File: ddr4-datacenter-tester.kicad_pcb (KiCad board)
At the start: 10 copper layers, 152.9 x 90 mm, 304 parts, among them IC1 TPS54561, IC3 TPD8S009DSMR, J1 0878311420, J10 61300311121, J3 DC_SOCKET, J4 WE_629105150521, J6 685119134923, J7 1140084168, J8 61300311121, Q2 BSS138APW, Q3 BSS138APW, Q4 BSS138APW, Q5 BSS138APW, Q6 BSS138APW, Q7 BSS138APW, Q8 BSS138APW, U10 LM3881MME_NOPB, U11 S27KL0641DABHI023, U12 TPS62823DLCT, U14 2199155-1, U15 XC7K160T-FFG676, U3 S25FL128SAGNFI000, U4 TPS65296, U5 TPS62823DLCT, U6 KSZ9031RNXCA, U7 FT4232HQ, U8 SRST, U9 TPS62823DLCT, Y1 ABM8G-25.000MHZ-18-D2Y-T, Y2 ABM8G-12.000MHZ-18-D2Y-T

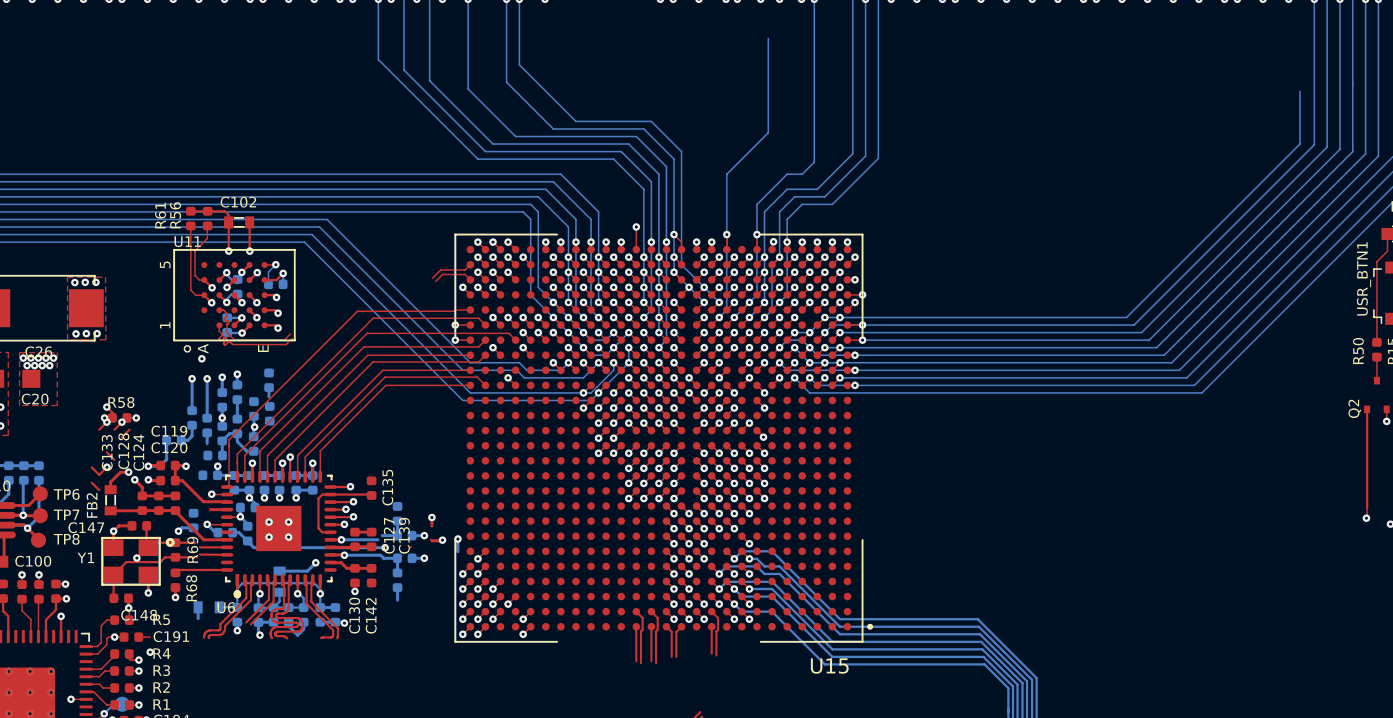
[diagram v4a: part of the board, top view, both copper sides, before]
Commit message: Add hyper ram routing
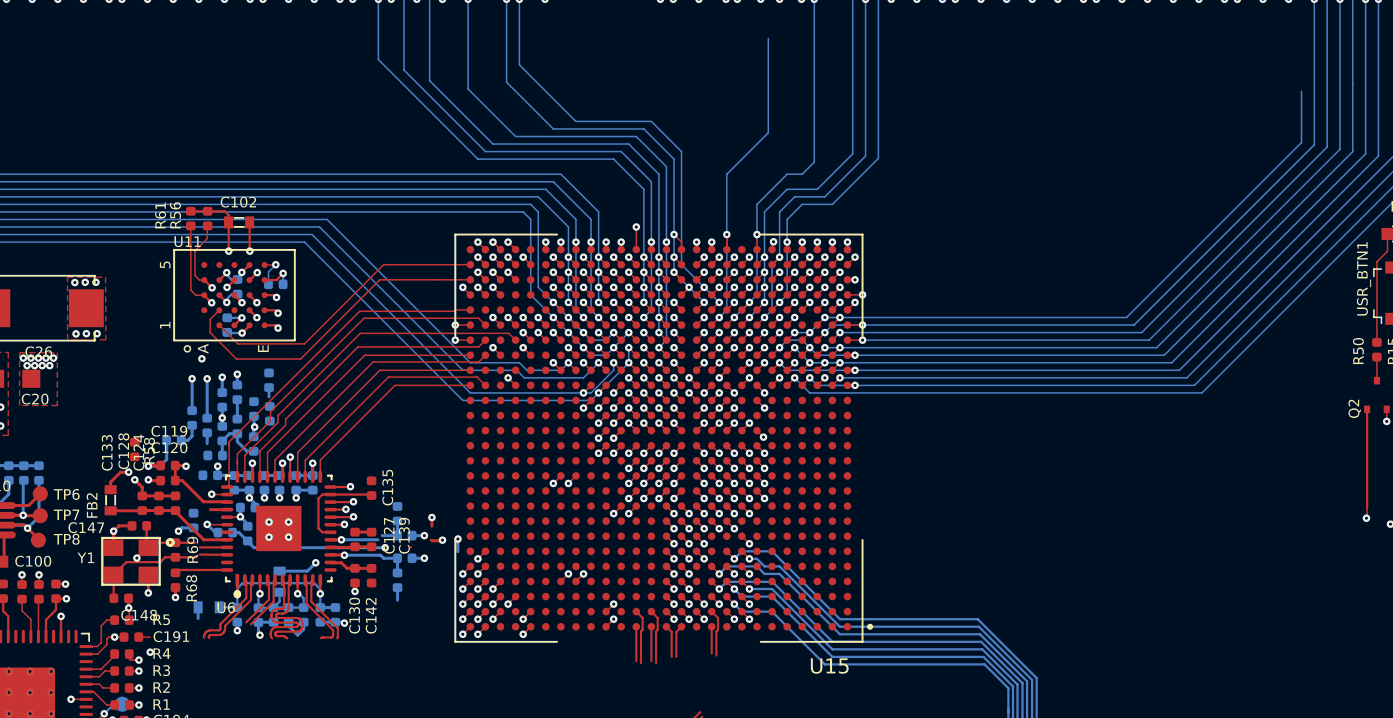
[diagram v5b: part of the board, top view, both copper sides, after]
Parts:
- moved R58 2.32 mm to (148.9, 90.8), turned to 90 degrees
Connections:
- U15 pad AC8: Net-(U15-PadAC8) -> DQS17_T
- U15 pad AD8: Net-(U15-PadAD8) -> DQS17_C
- U15 pad B18: 3V3_SYS -> VDDQ
- U15 pad E19: 3V3_SYS -> VDDQ
- U15 pad F16: 3V3_SYS -> VDDQ
- U15 pad H20: 3V3_SYS -> VDDQ
- U15 pad J17: 3V3_SYS -> VDDQ
- U15 pad K24: 3V3_SYS -> VDDQ
- U15 pad M18: 3V3_SYS -> VDDQ
- U15 pad N25: 3V3_SYS -> VDDQ
- U15 pad P22: 3V3_SYS -> VDDQ
- U15 pad R19: 3V3_SYS -> VDDQ
- U15 pad T16: 3V3_SYS -> VDDQ
- U15 pad T26: 3V3_SYS -> VDDQ
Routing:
- net HR_CKP: track 9.49 -> 21.9 mm
- net HR_RST: track 19.6 -> 30.5 mm
- net HR_CKN: track 9.89 -> 19.3 mm
- net HR_RW: track 13.3 -> 22.7 mm
- net HR_DQ4: track 12.1 -> 21.4 mm
- net HR_CS: track 18.2 -> 26.9 mm
- net HR_DQ2: track 12.2 -> 20.9 mm
- net HR_DQ3: track 13.7 -> 22.4 mm
- net HR_DQ0: track 11.5 -> 19.8 mm
- net HR_DQ5: track 8.81 -> 16.4 mm, vias 3 -> 2
- net HR_DQ7: track 10.8 -> 17.8 mm
- net Net-(U15-PadAD4): track 20.3 -> 25.2 mm
- net HR_DQ6: track 12.2 -> 16.5 mm
- net Net-(U15-PadAE11): track 15.5 -> 11.7 mm
- net HR_DQ1: track 15.5 -> 18.3 mm
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
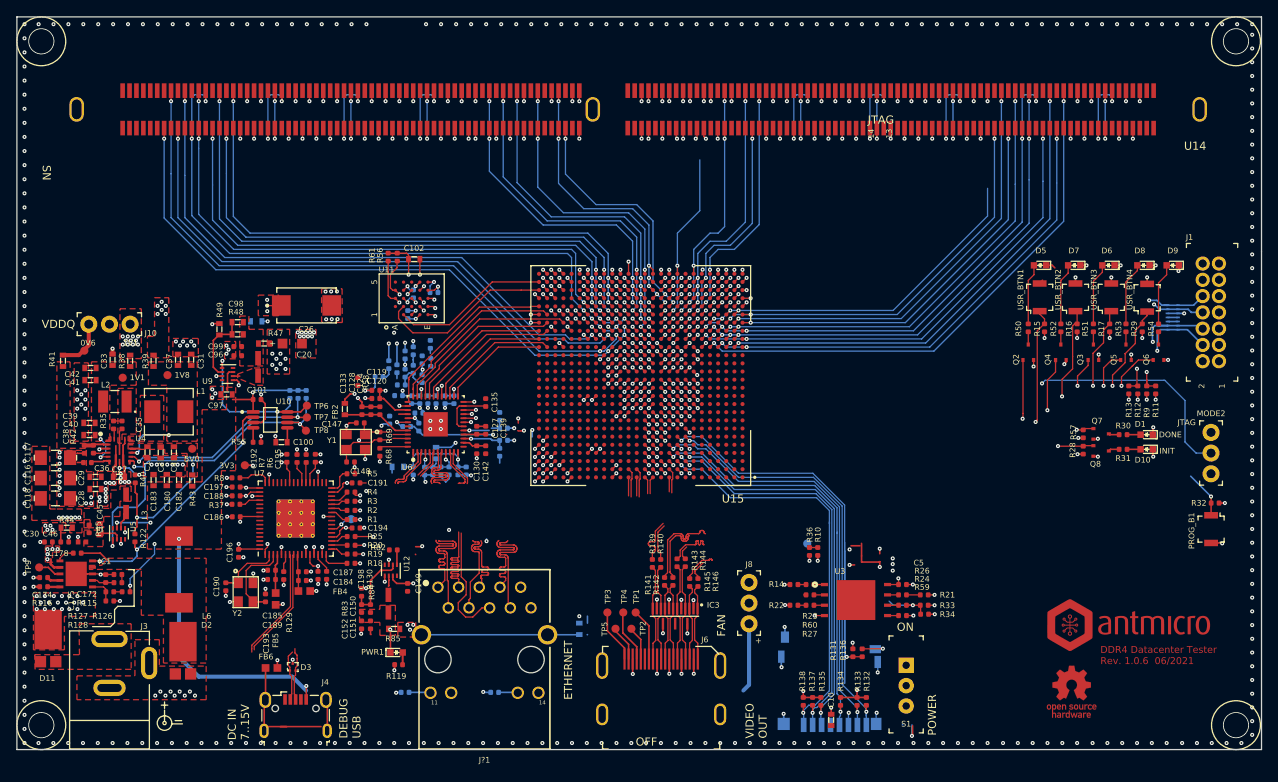
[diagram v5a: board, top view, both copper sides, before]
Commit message: Add DQS[9:17] redundant connection
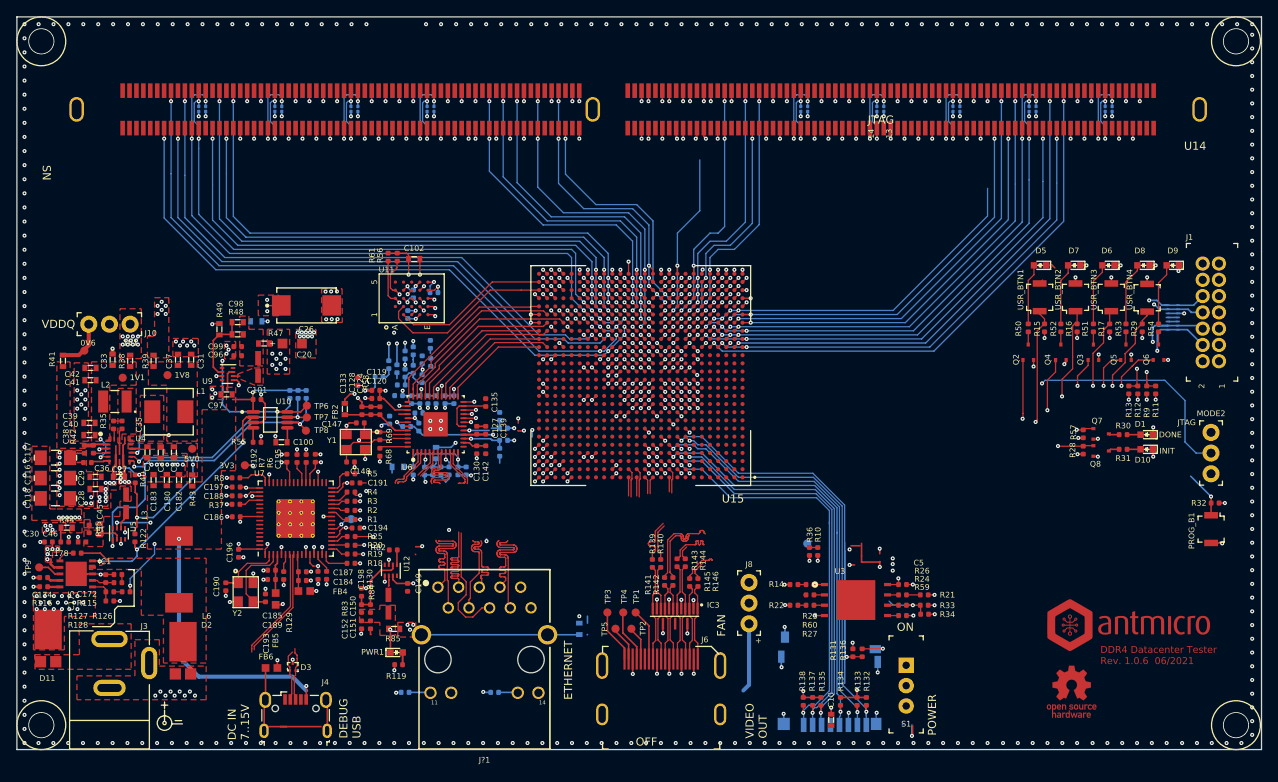
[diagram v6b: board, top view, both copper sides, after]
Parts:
- added R117: R_0R_0201, ddr4-datacenter-tester-footprints:0201-res, B.Cu at (130.2, 57.3)
- added R118: R_0R_0201, ddr4-datacenter-tester-footprints:0201-res, B.Cu at (129.3, 57.3)
- added R120: R_0R_0201, ddr4-datacenter-tester-footprints:0201-res, B.Cu at (148.9, 57.3)
- added R121: R_0R_0201, ddr4-datacenter-tester-footprints:0201-res, B.Cu at (148.0, 57.3)
- added R123: R_0R_0201, ddr4-datacenter-tester-footprints:0201-res, B.Cu at (158.2, 57.3)
- added R124: R_0R_0201, ddr4-datacenter-tester-footprints:0201-res, B.Cu at (157.4, 57.3)
- added R125: R_0R_0201, ddr4-datacenter-tester-footprints:0201-res, B.Cu at (139.5, 57.3)
- added R147: R_0R_0201, ddr4-datacenter-tester-footprints:0201-res, B.Cu at (138.7, 57.3)
- added R148: R_0R_0201, ddr4-datacenter-tester-footprints:0201-res, B.Cu at (241.5, 57.3)
- added R149: R_0R_0201, ddr4-datacenter-tester-footprints:0201-res, B.Cu at (240.7, 57.3)
- added R150: R_0R_0201, ddr4-datacenter-tester-footprints:0201-res, B.Cu at (213.5, 57.3)
- added R151: R_0R_0201, ddr4-datacenter-tester-footprints:0201-res, B.Cu at (212.6, 57.3)
- added R152: R_0R_0201, ddr4-datacenter-tester-footprints:0201-res, B.Cu at (232.2, 57.3)
- added R153: R_0R_0201, ddr4-datacenter-tester-footprints:0201-res, B.Cu at (231.3, 57.3)
- added R154: R_0R_0201, ddr4-datacenter-tester-footprints:0201-res, B.Cu at (222.8, 57.3)
- added R155: R_0R_0201, ddr4-datacenter-tester-footprints:0201-res, B.Cu at (222.0, 57.3)
- added R156: R_0R_0201, ddr4-datacenter-tester-footprints:0201-res, B.Cu at (204.1, 57.3)
- added R157: R_0R_0201, ddr4-datacenter-tester-footprints:0201-res, B.Cu at (203.3, 57.3)
- R100, R101, R102, R103, R104, R105, R106, R107, R108, R109, R110, R111, R112, R113, R114, R97, R98, R99: footprint antmicro-footprints:0201-res -> ddr4-datacenter-tester-footprints:0201-res
- U14: footprint antmicro-footprints:2199155-1 -> ddr4-datacenter-tester-footprints:2199155-1
- U15: footprint antmicro-footprints:BGA676C100P26X26_2700X2700X254 -> ddr4-datacenter-tester-footprints:BGA676C100P26X26_2700X2700X254
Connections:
- U15 pad AC8: DQS17_T -> Net-(R156-Pad2)
- U15 pad AD8: DQS17_C -> Net-(R157-Pad2)
- U15 pad N16: USR_BTN1 -> Net-(U15-PadN16)
- U15 pad N17: USR_LED1 -> Net-(U15-PadN17)
- U15 pad P16: USR_LED5 -> Net-(U15-PadP16)
- U15 pad R16: USR_LED2 -> Net-(R125-Pad1)
- U15 pad R17: USR_BTN4 -> Net-(R147-Pad1)
- U15 pad T17: USR_LED4 -> Net-(U15-PadT17)
- U15 pad T18: USR_BTN3 -> Net-(U15-PadT18)
- U15 pad U16: USR_LED3 -> Net-(U15-PadU16)
- U15 pad U17: USR_BTN2 -> Net-(U15-PadU17)
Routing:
- net Net-(R149-Pad1): track 0.71 -> 84.9 mm, vias 1 -> 2
- net Net-(R148-Pad1): track 0.71 -> 83.4 mm, vias 1 -> 2
- net Net-(R153-Pad1): track 0.71 -> 81.2 mm, vias 1 -> 2
- net Net-(R152-Pad1): track 0.71 -> 80.5 mm, vias 1 -> 2
- net Net-(R155-Pad1): track 0.71 -> 76.6 mm, vias 1 -> 2
- net Net-(R154-Pad1): track 0.71 -> 75.2 mm, vias 1 -> 2
- net Net-(R118-Pad1): track 0.00 -> 66.3 mm, vias 0 -> 2
- net Net-(R125-Pad1): track 0.00 -> 65.5 mm, vias 0 -> 2
- net Net-(R117-Pad1): track 0.00 -> 65.3 mm, vias 0 -> 2
- net Net-(R147-Pad1): track 0.00 -> 65.1 mm, vias 0 -> 2
- net Net-(R151-Pad1): track 0.71 -> 65.0 mm, vias 1 -> 2
- net Net-(R150-Pad1): track 0.71 -> 64.4 mm, vias 1 -> 2
- net Net-(R120-Pad1): track 0.00 -> 52.8 mm, vias 0 -> 2
- net Net-(R121-Pad1): track 0.00 -> 52.4 mm, vias 0 -> 2
- net Net-(R123-Pad1): track 0.00 -> 37.8 mm, vias 0 -> 2
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
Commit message: Update layer stack table
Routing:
- added copper zone on In5.Cu, net GND
- removed copper zone on In4_LS.Cu, net GND
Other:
- board text added: "0.13 mm"
- board text added: "18"
- board text added: "19"
- board text added: "20"
- board text added: "21"
- board text added: "Dielectric 8"
- board text added: "Dielectric 9"
- board text added: "In4.Cu"
- board text added: "In7.Cu"
- board text removed: "0.018 mm"
- board text removed: "0.23 mm"
